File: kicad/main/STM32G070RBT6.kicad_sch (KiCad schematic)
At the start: 35 parts, among them U13 STM32G473VCT6, X1 ABM3-8_000MHZ-D2Y-T

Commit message: Side sensor VL6180
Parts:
- removed R82, R85, R86, R87: 10, symbol Device:R_US
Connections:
- net PC14: now also MCU_IO1.13 (Pin_13); no longer MCU_IO1.5 (Pin_5)
- net PC15: now also MCU_IO1.15 (Pin_15); no longer MCU_IO1.7 (Pin_7)
- net PD8: now also MCU_IO1.19 (Pin_19); no longer MCU_IO1.9 (Pin_9)
- net PD9: now also MCU_IO1.21 (Pin_21); no longer MCU_IO1.11 (Pin_11)
- net PE0: now also MCU_IO1.25 (Pin_25); no longer MCU_IO1.13 (Pin_13)
- net PE1: now also MCU_IO1.27 (Pin_27); no longer MCU_IO1.15 (Pin_15)
- net PE10: now also MCU_IO1.35 (Pin_35); no longer MCU_IO1.31 (Pin_31)
- net PE11: now also MCU_IO1.37 (Pin_37); no longer MCU_IO1.33 (Pin_33)
- net PE12: now also MCU_IO1.39 (Pin_39); no longer MCU_IO1.35 (Pin_35)
- net PE13: now also MCU_IO1.41 (Pin_41); no longer MCU_IO1.37 (Pin_37)
- net PE14: now also MCU_IO1.43 (Pin_43); no longer MCU_IO1.39 (Pin_39)
- net PE15: now also MCU_IO1.45 (Pin_45); no longer MCU_IO1.41 (Pin_41)
- net PE6: now also MCU_IO1.29 (Pin_29); no longer MCU_IO1.25 (Pin_25)
- net PE7: now also MCU_IO1.31 (Pin_31); no longer MCU_IO1.27 (Pin_27)
- net PE8: now also MCU_IO1.33 (Pin_33); no longer MCU_IO1.29 (Pin_29)
- net PF2: now also MCU_IO1.47 (Pin_47); no longer MCU_IO1.43 (Pin_43)
- net SIDE-BRUSH-IN1: now also U13.10 (PF9); no longer U13.65 (PC6)
- net SIDE-BRUSH-IN2: now also U13.11 (PF10); no longer U13.66 (PC7)
- net USART2-IR-L-RX: now also U13.88 (PD6)
- net USART4-IR-R-RX: now also U13.80 (PC11)
- net VCC-3V3-P: now also MCU_IO1.5 (Pin_5), MCU_IO1.7 (Pin_7); no longer MCU_IO1.3 (Pin_3)
- net VCC-5V-REG: now also MCU_IO1.3 (Pin_3)
- net PD5: now reaches U13.87 (PD5)
- net PD5: now also MCU_IO1.17 (Pin_17)
- net PB10: now reaches U13.47 (PB10)
- net PB10: now also MCU_IO1.23 (Pin_23)
- net PC13: now reaches U13.7 (PC13)
- net PC13: now also MCU_IO1.11 (Pin_11)
- net PC10: now reaches U13.79 (PC10)
- net PC10: now also MCU_IO1.9 (Pin_9)
- net PE2 renamed SIDE-PROXI-GPIO-R
- net SIDE-PROXI-GPIO-R: no longer MCU_IO1.17 (Pin_17)
- net PE3 renamed SIDE-PROXI-CE-R
- net SIDE-PROXI-CE-R: no longer MCU_IO1.19 (Pin_19)
- net PE4 renamed SIDE-PROXI-GPIO-L
- net SIDE-PROXI-GPIO-L: no longer MCU_IO1.21 (Pin_21)
- net PE5 renamed SIDE-PROXI-CE-L
- net SIDE-PROXI-CE-L: no longer MCU_IO1.23 (Pin_23)
- removed net PF10: MCU_IO1.47 (Pin_47), U13.11 (PF10)
- removed net PF9: MCU_IO1.45 (Pin_45), U13.10 (PF9)
- new net I2C4_SCL: U13.65 (PC6)
- new net I2C4_SDA: U13.66 (PC7)
- no-connect marks 10 -> 8

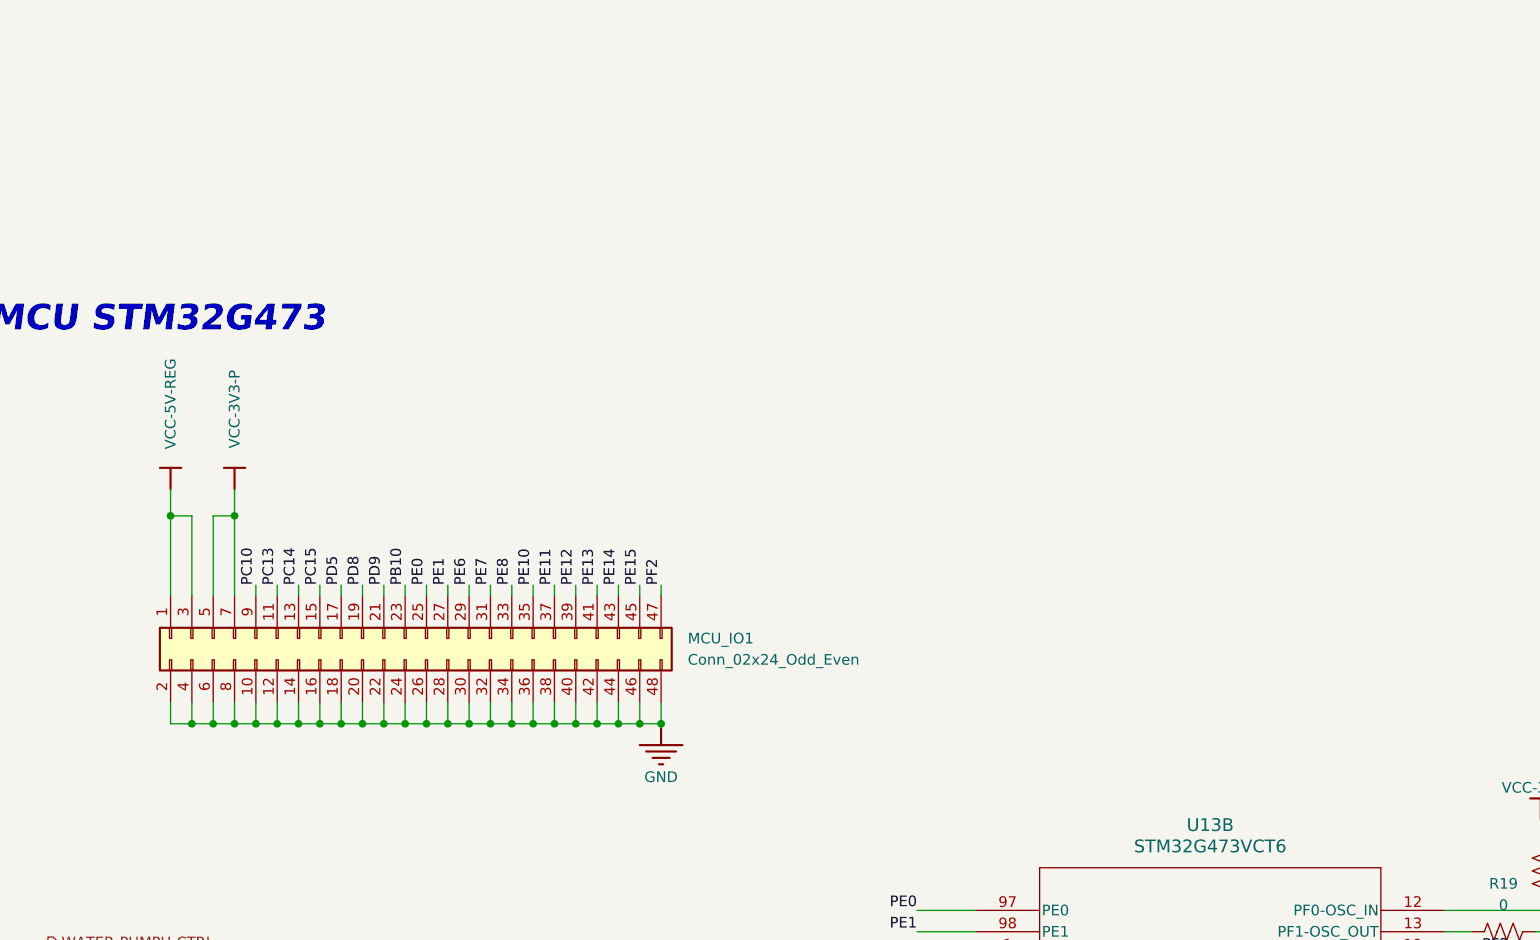
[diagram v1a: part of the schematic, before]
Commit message: Fix edge cut; no-CM STEP
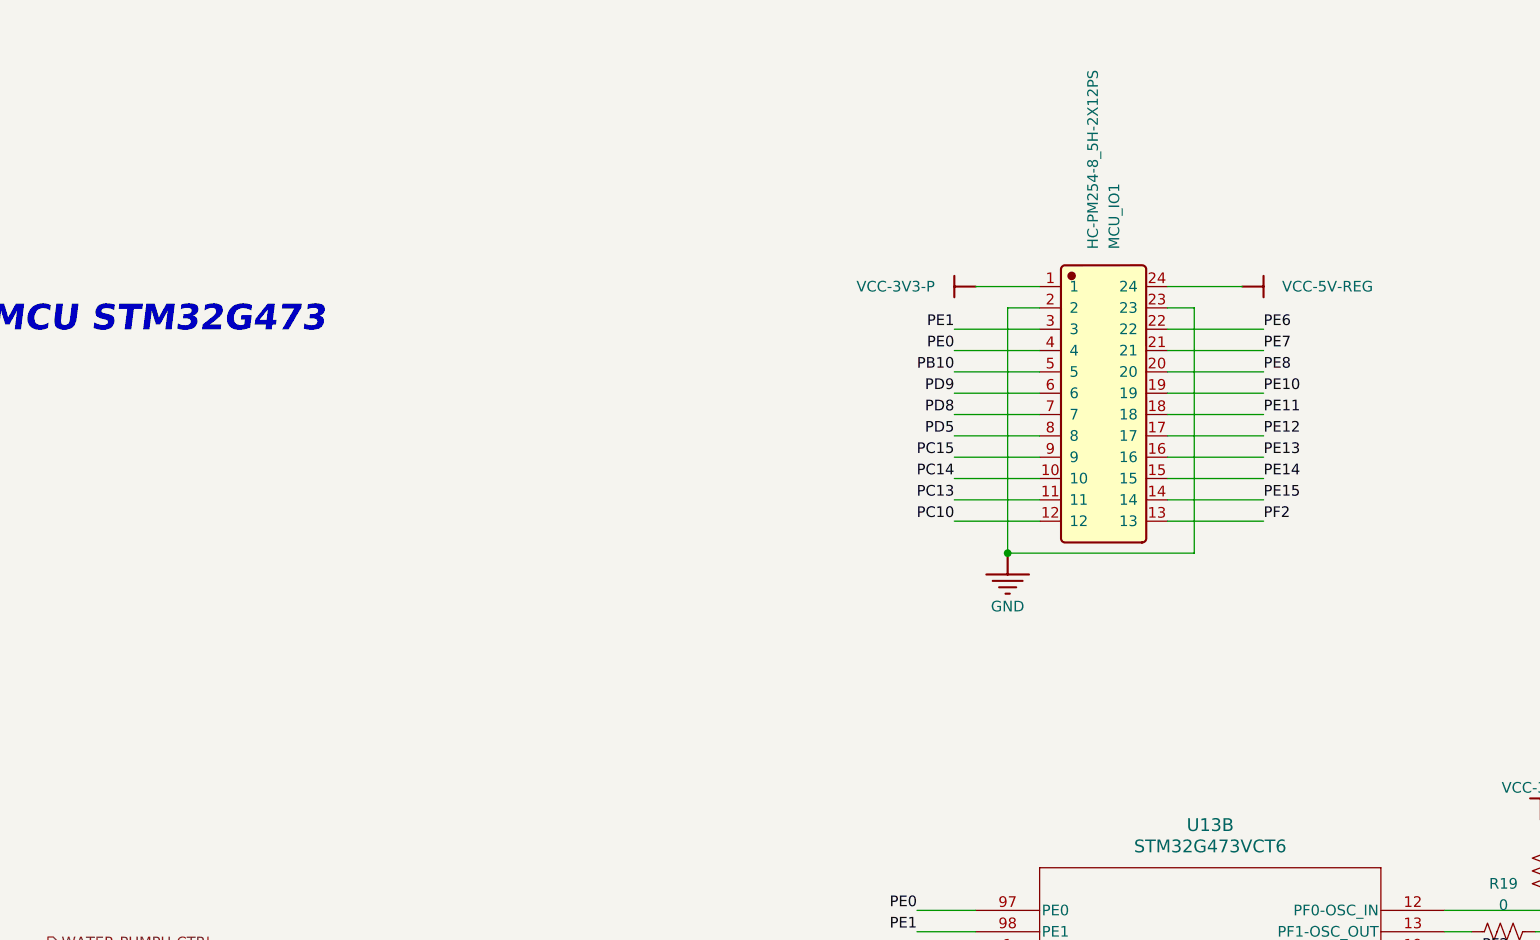
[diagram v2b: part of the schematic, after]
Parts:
- removed MCU_IO1: Conn_02x24_Odd_Even, symbol Connector_Generic:Conn_02x24_Odd_Even
- added MCU_IO1: HC-PM254-8_5H-2X12PS, JLCImport:HC-PM254-8_5H-2X12PS, symbol JLCImport:HC-PM254-8_5H-2X12PS
- R113, R117, R64, R73, R74, R80, R94, R95: footprint (none) -> Resistor_SMD:R_0603_1608Metric
- R16: footprint Resistor_SMD:R_0603_1608Metric -> Resistor_SMD:R_1206_3216Metric
- STM_DEBUG1: footprint (none) -> Connector_PinHeader_2.54mm:PinHeader_1x05_P2.54mm_Vertical
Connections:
- net GND: now also MCU_IO1.2, MCU_IO1.23
- net PB10: now also MCU_IO1.5
- net PC10: now also MCU_IO1.12
- net PC13: now also MCU_IO1.11
- net PC14: now also MCU_IO1.10
- net PC15: now also MCU_IO1.9
- net PD5: now also MCU_IO1.8
- net PD8: now also MCU_IO1.7
- net PD9: now also MCU_IO1.6
- net PE0: now also MCU_IO1.4
- net PE1: now also MCU_IO1.3
- net PE10: now also MCU_IO1.19
- net PE11: now also MCU_IO1.18
- net PE12: now also MCU_IO1.17
- net PE13: now also MCU_IO1.16
- net PE14: now also MCU_IO1.15
- net PE15: now also MCU_IO1.14
- net PE6: now also MCU_IO1.22
- net PE7: now also MCU_IO1.21
- net PE8: now also MCU_IO1.20
- net PF2: now also MCU_IO1.13
- net VCC-3V3-P: now also MCU_IO1.1
- net VCC-5V-REG: now also MCU_IO1.24

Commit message: Schematic fixes, 1st round of review
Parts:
- removed R16: 0.01, Resistor_SMD:R_1206_3216Metric, symbol Device:R_US
- added C39, C42: 18pF/10V, Capacitor_SMD:C_0603_1608Metric, symbol Device:C_Small
- added X3: XKXEL89CII-SUAYLC-32_768K, JLCImport:XKXEL89CII-SUAYLC-32_768K, symbol JLCImport:XKXEL89CII-SUAYLC-32_768K
- C12, C13, C14, C15, C16, C30, C32, C37: value 100nF/10V -> 100nF/50V; LCSC (none) -> C1591
- C17, C31, C33: value 4.7uF/10V -> 10uF/25V; LCSC (none) -> C96446
- C34, C35: value 22pF/10V -> 22pF/50V
- D5: LCSC (none) -> C22448055
- R113: value 10 -> 1k
- STM_DEBUG1: LCSC (none) -> C42431835
- U13: LCSC (none) -> C730121
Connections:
- net GND: now also C39.1, C42.1
- net 3.3VBAT: now reaches U13.6 (VBAT)
- net MAIN-FAN-V-CTRL renamed CLEAN-BTN
- net PC14: no longer names the net of MCU_IO1.10
- net PC14: no longer U13.8 (PC14-OSC32_IN)
- net PC15: no longer names the net of MCU_IO1.9
- net PC15: no longer U13.9 (PC15-OSC32_OUT)
- net PD8: no longer names the net of MCU_IO1.7
- net PD8: no longer U13.55 (PD8)
- net PD9: no longer names the net of MCU_IO1.6
- net PD9: no longer U13.56 (PD9)
- net STM32-RST renamed ~{STM32_RST}
- net ~{STM32_RST}: no longer JTAG1.12
- new net: C42.2, U13.8 (PC14-OSC32_IN), X3.2 (OSC2)
- new net: C39.2, U13.9 (PC15-OSC32_OUT), X3.1 (OSC1)
- new net LIDAR_EN: U13.56 (PD9)
- new net WDO: U13.55 (PD8)
- new net ~{JTAG_RST}: JTAG1.12
- no-connect marks 8 -> 12
